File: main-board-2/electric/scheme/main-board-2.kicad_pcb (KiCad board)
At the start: 2 copper layers, 85 x 56 mm, 126 parts, among them K1 power-switch, K2 usb-power-switch, P1 batt, P10 screw-3, P11 screw-1, P12 screw-4, P13 screw-2, P14 gpio-big, P15 gpio-small, P16 moto-1, P17 moto-2, P2 CONN_4, P3 trigger-btn, P4 CONN_3X2, P5 reg-short-to-gnd-1, P6 reg-short-to-gnd-2, P7 bootloader, P8 cross board conn, P9 rst, Q1 IRLML2244, Q10 IRLML2244, Q11 sot223, Q12 bc857, Q13 irlml2244, Q2 BC847, Q3 IRLML2244, Q4 IRLML2244, Q5 BC847, Q6 BC847, Q7 BC847, Q8 BC847, Q9 IRLML2244, U1 LM317AEMP, U2 LM317AT, U3 LM317AEMP, U4 LM317AT, U5 LM293, U6 L298, U7 MINI-USB-B, X1 8MHz

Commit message: Placing components...
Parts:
- moved P2 21.8 mm to (159.4, 179.6), turned to 180 degrees
- moved R31 6.89 mm to (203.6, 172.7)
- moved Q10 6.89 mm to (203.7, 170.2)
- moved Q8 6.89 mm to (200.3, 173.5)
- moved R26 6.89 mm to (195.2, 173.5)
- moved R27 6.89 mm to (197.1, 173.5)
- moved R30 6.89 mm to (200.7, 170.9)
- moved Q7 3.70 mm to (211.8, 156.4)
- moved Q9 3.70 mm to (209.5, 150.8)
- moved R25 3.70 mm to (206.4, 160.0)
- moved R28 3.70 mm to (208.5, 156.1)
- moved R29 3.70 mm to (210.0, 160.0)
- moved Q11 3.62 mm to (209.4, 150.2)
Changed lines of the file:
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@@
   )
   (module SOT23GDS (layer B.Cu)
-    (at 204.343 163.322)
+    (at 203.708 170.18)
     (descr "Module CMS SOT23 Transistore EBC")
     (tags "CMS SOT")
@@
   )
   (module SOT23GDS (layer B.Cu)
-    (at 206.3115 148.9075)
+    (at 209.4865 150.8125)
     (descr "Module CMS SOT23 Transistore EBC")
     (tags "CMS SOT")
@@
   )
   (module SOT23EBC (layer B.Cu)
-    (at 208.5975 154.4955)
+    (at 211.7725 156.4005)
     (descr "Module CMS SOT23 Transistore EBC")
     (tags "CMS SOT")
@@
   )
   (module SOT23EBC (layer B.Cu)
-    (at 200.914 166.624 270)
+    (at 200.279 173.482 270)
     (descr "Module CMS SOT23 Transistore EBC")
     (tags "CMS SOT")
@@
   )
   (module SOT223-GDSD   placed (layer B.Cu)
-    (at 206.3115 148.3995 180)
+    (at 209.423 150.241 180)
     (descr "module CMS SOT223 4 pins")
     (tags "CMS SOT")
@@
   )
   (module SM0805 (layer B.Cu)
-    (at 203.2635 158.0515 180)
+    (at 206.4385 159.9565 180)
     (attr smd)
     (fp_text reference R25 (at 0 0.3175 180) (layer B.SilkS)
@@
   )
   (module SM0805 (layer B.Cu)
-    (at 197.739 166.624 270)
+    (at 197.104 173.482 270)
     (attr smd)
     (fp_text reference R27 (at 0 0.3175 270) (layer B.SilkS)
@@
   )
   (module SM0805 (layer B.Cu)
-    (at 206.8195 158.0515 180)
+    (at 209.9945 159.9565 180)
     (attr smd)
     (fp_text reference R29 (at 0 0.3175 180) (layer B.SilkS)
@@
   )
   (module SM0805 (layer B.Cu)
-    (at 195.834 166.624 270)
+    (at 195.199 173.482 270)
     (attr smd)
     (fp_text reference R26 (at 0 0.3175 270) (layer B.SilkS)
@@
   )
   (module SM0805 (layer B.Cu)
-    (at 204.216 165.862)
+    (at 203.581 172.72)
     (attr smd)
     (fp_text reference R31 (at 0 0.3175) (layer B.SilkS)
@@
   )
   (module SM0805 (layer B.Cu)
-    (at 205.2955 154.2415)
+    (at 208.4705 156.1465)
     (attr smd)
     (fp_text reference R28 (at 0 0.3175) (layer B.SilkS)
@@
   )
   (module SM0805 (layer B.Cu)
-    (at 201.295 164.084 180)
+    (at 200.66 170.942 180)
     (attr smd)
     (fp_text reference R30 (at 0 0.3175 180) (layer B.SilkS)
@@
   )
   (module PIN_ARRAY_4x1 (layer F.Cu)
-    (at 153.543 200.533)
+    (at 159.385 179.578 180)
     (descr "Double rangee de contacts 2 x 5 pins")
     (tags CONN)
-    (fp_text reference P2 (at 0 -2.54) (layer F.SilkS)
+    (fp_text reference P2 (at 0 -2.54 180) (layer F.SilkS)
       (effects (font (size 1.016 1.016) (thickness 0.2032)))
     )
-    (fp_text value CONN_4 (at 0 2.54) (layer F.SilkS) hide
+    (fp_text value CONN_4 (at 0 2.54 180) (layer F.SilkS) hide
       (effects (font (size 1.016 1.016) (thickness 0.2032)))
     )
@@
     (fp_line (start -5.08 -1.27) (end -5.08 1.27) (layer F.SilkS) (width 0.254))
     (fp_line (start 5.08 1.27) (end 5.08 -1.27) (layer F.SilkS) (width 0.254))
-    (pad 1 thru_hole rect (at -3.81 0) (size 1.524 1.524) (drill 1.016)
+    (pad 1 thru_hole rect (at -3.81 0 180) (size 1.524 1.524) (drill 1.016)
       (layers *.Cu *.Mask F.SilkS)
       (net 6 /batt+)
     )
-    (pad 2 thru_hole circle (at -1.27 0) (size 1.524 1.524) (drill 1.016)
+    (pad 2 thru_hole circle (at -1.27 0 180) (size 1.524 1.524) (drill 1.016)
       (layers *.Cu *.Mask F.SilkS)
       (net 1 /+5V)
     )
-    (pad 3 thru_hole circle (at 1.27 0) (size 1.524 1.524) (drill 1.016)
+    (pad 3 thru_hole circle (at 1.27 0 180) (size 1.524 1.524) (drill 1.016)
       (layers *.Cu *.Mask F.SilkS)
       (net 83 VDD)
     )
-    (pad 4 thru_hole circle (at 3.81 0) (size 1.524 1.524) (drill 1.016)
+    (pad 4 thru_hole circle (at 3.81 0 180) (size 1.524 1.524) (drill 1.016)
       (layers *.Cu *.Mask F.SilkS)
       (net 45 GND)

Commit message: Placing components...
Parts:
- moved Q12 30.1 mm to (160.4, 169.3)
- moved W10 30.1 mm to (157.0, 165.7)
- moved R47 30.1 mm to (156.1, 169.3)
- moved Q13 30.1 mm to (160.7, 165.6)
- moved R48 30.1 mm to (163.3, 165.6)
- moved R46 30.1 mm to (157.9, 169.3)
- moved R49 30.1 mm to (161.8, 162.8)
- moved R35 4.20 mm to (161.4, 176.1)
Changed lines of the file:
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@@
   )
   (module SOT23GDS (layer B.Cu)
-    (at 131.318 159.004)
+    (at 160.655 165.608)
     (descr "Module CMS SOT23 Transistore EBC")
     (tags "CMS SOT")
@@
   )
   (module SOT23EBC (layer B.Cu)
-    (at 131.064 162.687 270)
+    (at 160.401 169.291 270)
     (descr "Module CMS SOT23 Transistore EBC")
     (tags "CMS SOT")
@@
   )
   (module SM0805 (layer B.Cu)
-    (at 128.524 162.687 270)
+    (at 157.861 169.291 270)
     (attr smd)
     (fp_text reference R46 (at 0 0.3175 270) (layer B.SilkS)
@@
   )
   (module SM0805 (layer F.Cu)
-    (at 157.607 177.927 180)
+    (at 161.417 176.149 180)
     (attr smd)
     (fp_text reference R35 (at 0 -0.3175 180) (layer F.SilkS)
@@
   )
   (module SM0805 (layer B.Cu)
-    (at 133.985 159.004 90)
+    (at 163.322 165.608 90)
     (attr smd)
     (fp_text reference R48 (at 0 0.3175 90) (layer B.SilkS)
@@
   )
   (module SM0805 (layer B.Cu)
-    (at 126.746 162.687 270)
+    (at 156.083 169.291 270)
     (attr smd)
     (fp_text reference R47 (at 0 0.3175 270) (layer B.SilkS)
@@
   )
   (module PIN_ARRAY_2X1 (layer B.Cu)
-    (at 127.635 159.131 90)
+    (at 156.972 165.735 90)
     (descr "Connecteurs 2 pins")
     (tags "CONN DEV")
@@
   )
   (module SM0805 (layer B.Cu)
-    (at 132.461 156.21 180)
+    (at 161.798 162.814 180)
     (attr smd)
     (fp_text reference R49 (at 0 0.3175 180) (layer B.SilkS)

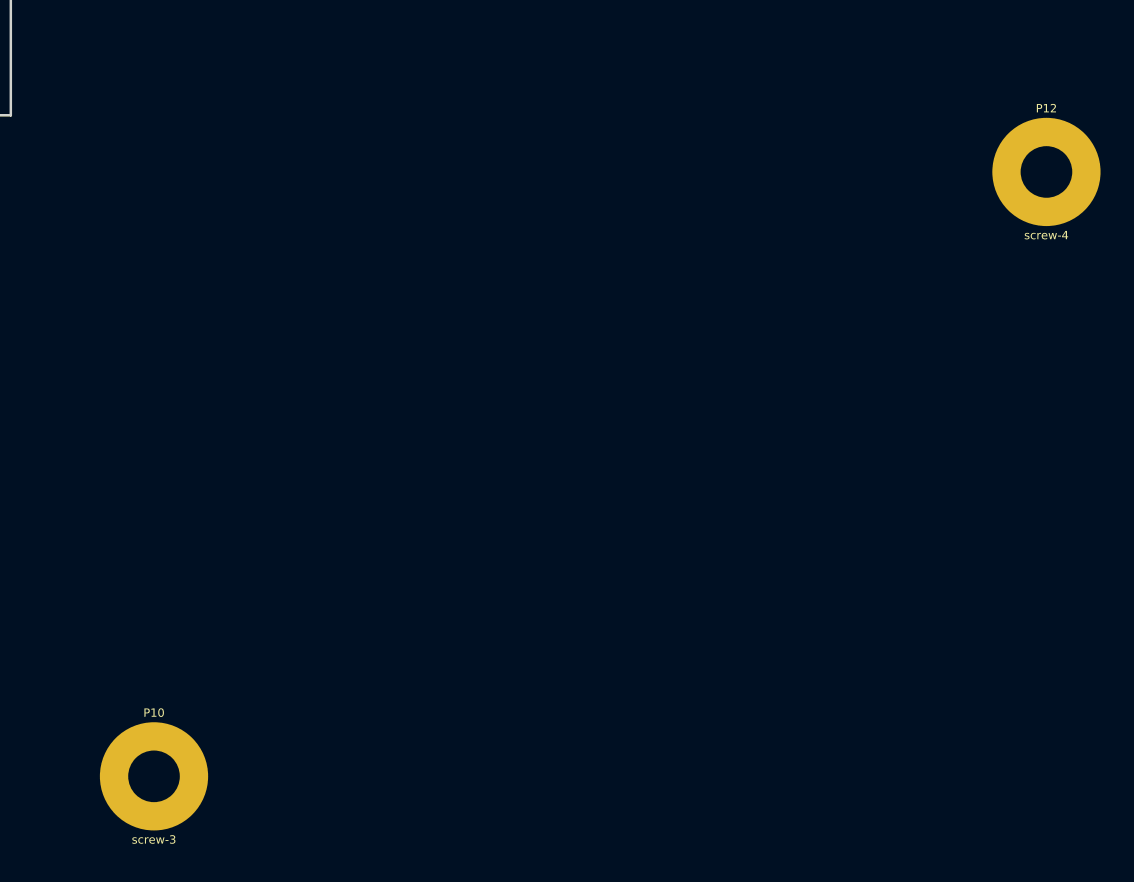
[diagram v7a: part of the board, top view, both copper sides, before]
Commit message: Removed unused screw holes.
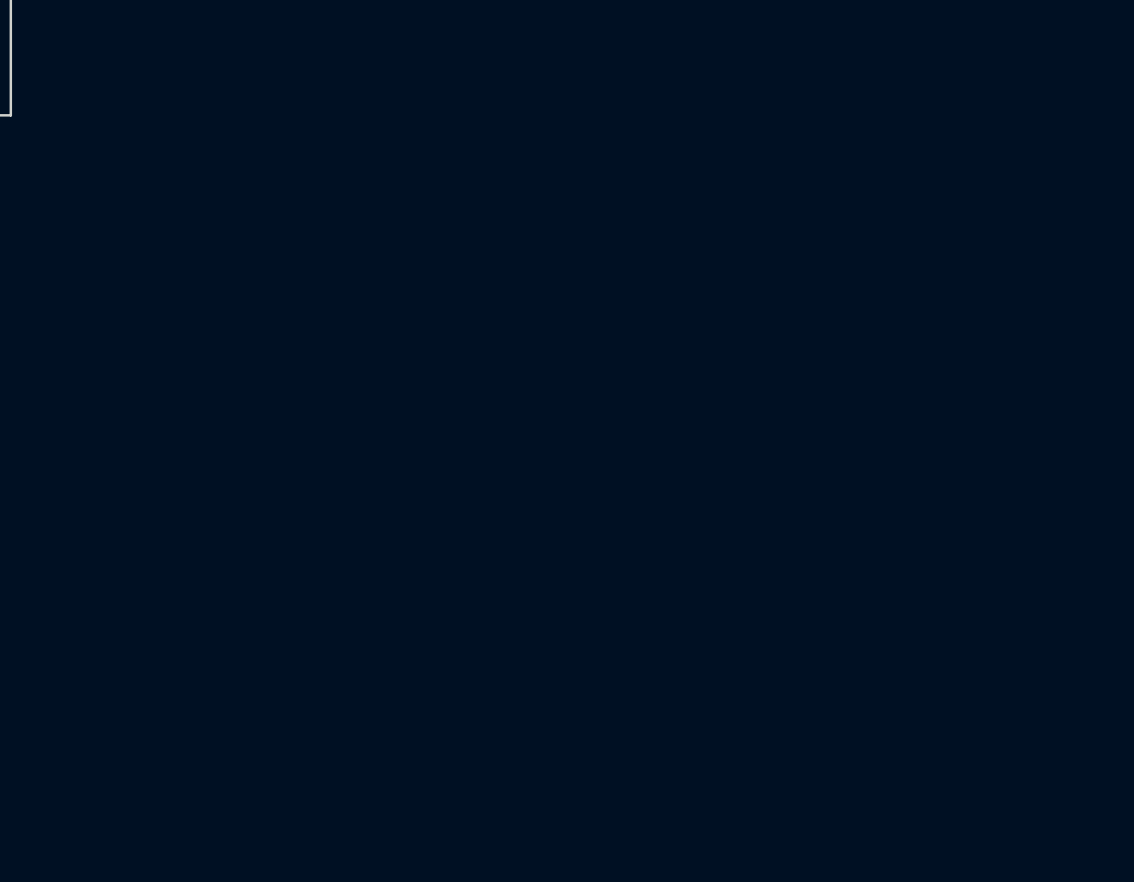
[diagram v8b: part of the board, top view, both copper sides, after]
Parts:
- removed P10: screw-3, m3-screw-hole
- removed P12: screw-4, m3-screw-hole
